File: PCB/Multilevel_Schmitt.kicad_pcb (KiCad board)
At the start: 2 copper layers, 55 x 70 mm, 26 parts, among them J1 Analog IO, J2 I2C input, J3 Conn_01x08_Female, J4 Conn_01x08_Female, J5 Conn_01x02_Female, U1 ATtiny84-20PU, U2 74HC14, U3 MCP1700-2502E_TO92, U4 74HC4051, U5 74HC4051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

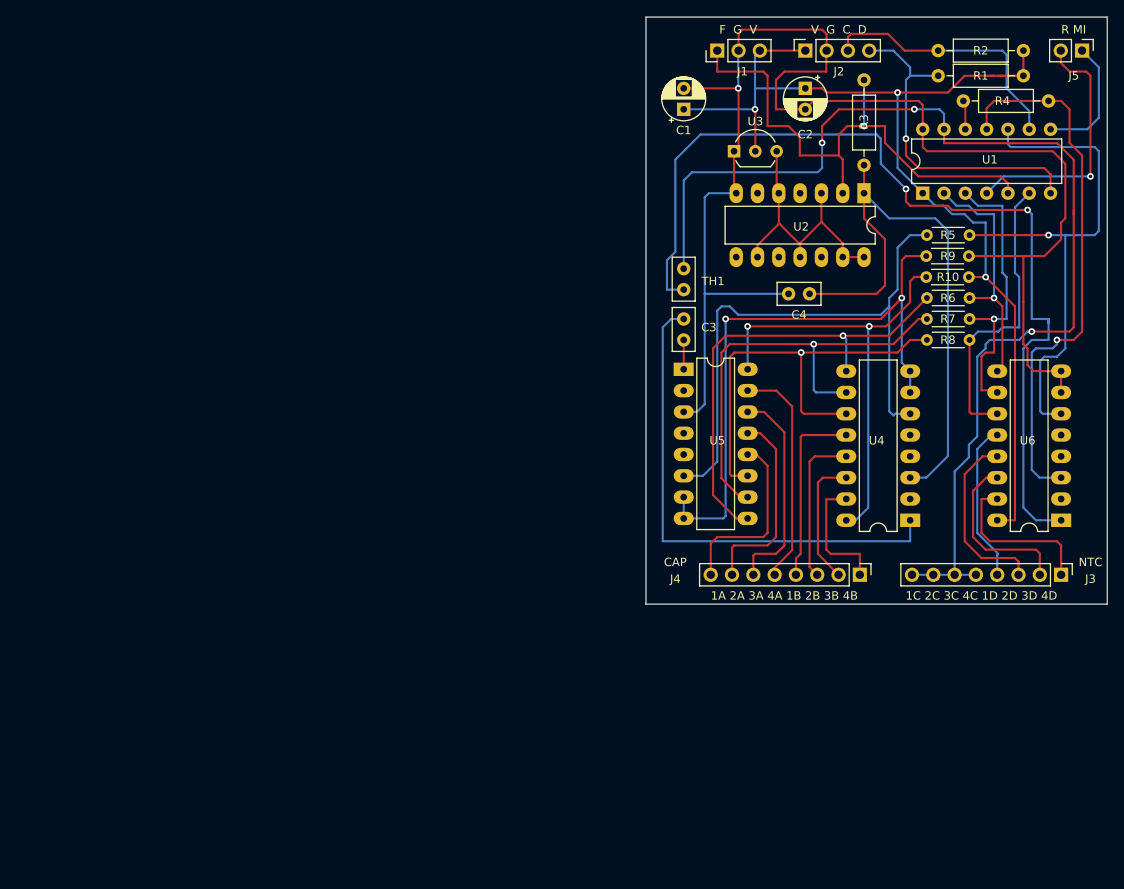
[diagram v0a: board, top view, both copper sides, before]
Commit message: Updates PCB design files, removed casing files and updates readme files
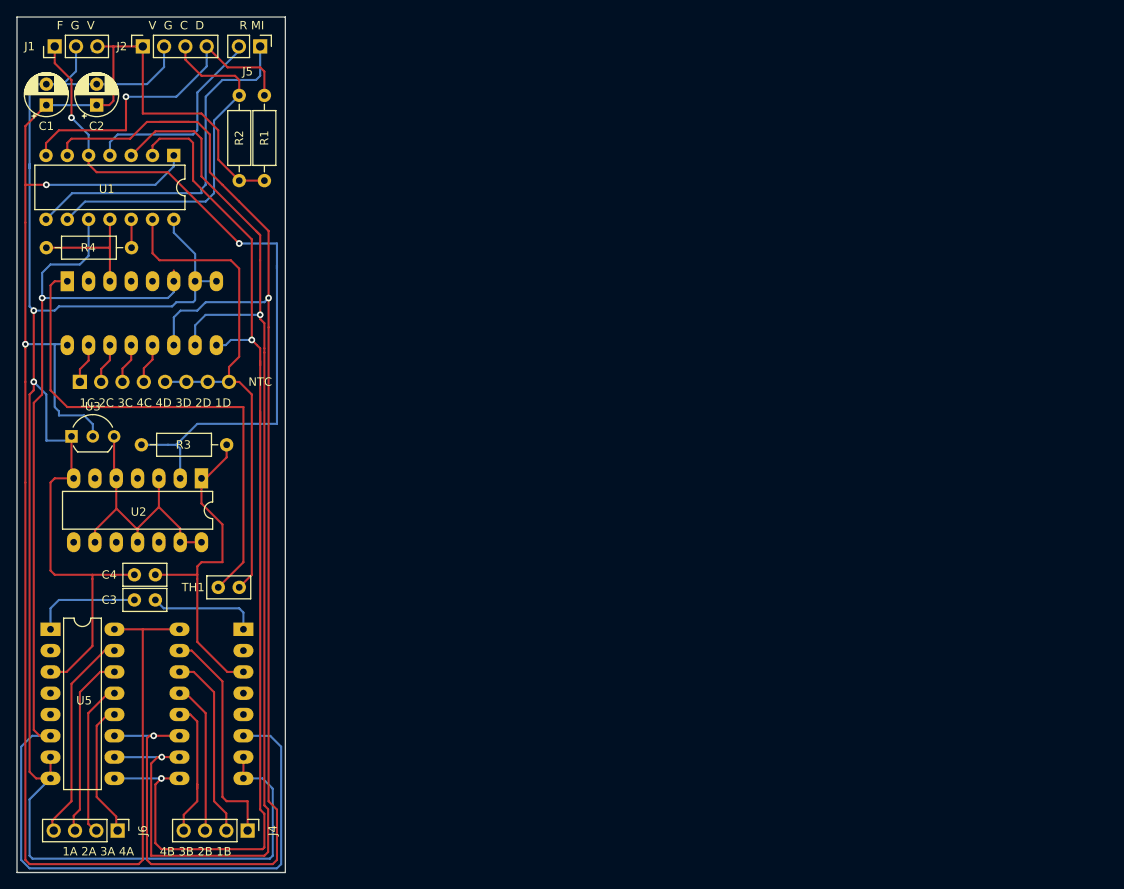
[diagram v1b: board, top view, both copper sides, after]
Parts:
- removed R10, R5, R6, R7, R8, R9: R, Resistor_THT:R_Axial_DIN0204_L3.6mm_D1.6mm_P5.08mm_Horizontal
- added J6: Conn_01x04_Female, Connector_PinHeader_2.54mm:PinHeader_1x04_P2.54mm_Vertical, F.Cu at (112.0, 147.0)
- J3, U4, U6: moved to B.Cu
- J4: value Conn_01x08_Female -> Conn_01x04_Female; footprint Connector_PinHeader_2.54mm:PinHeader_1x08_P2.54mm_Vertical -> Connector_PinHeader_2.54mm:PinHeader_1x04_P2.54mm_Vertical
- moved U6 121.9 mm to (106.0, 81.5), turned to 270 degrees
- moved R4 120.8 mm to (103.5, 77.5), turned to 0 degrees
- moved J3 119.2 mm to (107.5, 93.5)
- moved J5 98.0 mm to (129.0, 53.5)
- moved R2 94.8 mm to (126.5, 69.5), turned to 90 degrees
- moved R1 91.4 mm to (129.5, 69.5), turned to 90 degrees
- moved U1 89.4 mm to (118.7, 66.5), turned to 270 degrees
- moved U2 86.0 mm to (122.0, 105.0)
- moved U3 86.0 mm to (106.5, 100.0)
- moved C4 84.9 mm to (116.5, 116.5)
- moved C2 84.5 mm to (109.5, 60.5), turned to 90 degrees
- moved R3 83.0 mm to (125.0, 101.0), turned to 180 degrees
- moved U5 81.6 mm to (104.0, 123.0)
- moved U4 80.6 mm to (127.0, 123.0)
- moved J4 79.1 mm to (127.5, 147.0)
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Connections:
- U4 pad 10: Net-(R7-Pad1) -> S1
- U4 pad 11: Net-(R8-Pad1) -> S0
- U4 pad 16: 3V3 -> +3V3
- U4 pad 6: Net-(R5-Pad1) -> E
- U4 pad 7: GND2 -> M0
- U4 pad 8: GND2 -> M0
- U4 pad 9: Net-(R6-Pad1) -> S2
- U5 pad 10: Net-(R7-Pad1) -> S1
- U5 pad 11: Net-(R8-Pad1) -> S0
- U5 pad 12: Net-(J4-Pad8) -> Net-(J6-Pad1)
- U5 pad 13: Net-(J4-Pad7) -> Net-(J6-Pad2)
- U5 pad 14: Net-(J4-Pad6) -> Net-(J6-Pad3)
- U5 pad 15: Net-(J4-Pad5) -> Net-(J6-Pad4)
- U5 pad 16: 3V3 -> +3V3
- U5 pad 6: Net-(R5-Pad1) -> E
- U5 pad 7: GND2 -> M0
- U5 pad 8: GND2 -> M0
- U5 pad 9: Net-(R6-Pad1) -> S2
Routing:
- net S0: track 35.7 -> 168.1 mm, vias 0 -> 2
- net S1: track 35.8 -> 144.1 mm, vias 1 -> 2
- net +3V3: track 127.6 -> 229.1 mm, vias 3 -> 2
- net S2: track 29.4 -> 129.7 mm, vias 1 -> 2
- net E: track 63.8 -> 155.8 mm
- net M0: track 176.7 -> 256.8 mm, vias 1 -> 2
- net NTC_H: track 136.5 -> 63.7 mm, vias 3 -> 0
- net GND2: track 72.5 -> 0.00 mm, vias 2 -> 0
- net Net-(R5-Pad1): track 71.9 -> 0.00 mm
- net Net-(R7-Pad1): track 55.4 -> 0.00 mm, vias 1 -> 0
- net Net-(R6-Pad1): track 55.3 -> 0.00 mm, vias 1 -> 0
- net 3V3: track 55.2 -> 0.00 mm, vias 2 -> 0
- net Net-(R8-Pad1): track 53.0 -> 0.00 mm, vias 1 -> 0
- net TR: track 113.3 -> 61.3 mm, vias 2 -> 0
- net A5: track 66.2 -> 15.0 mm, vias 1 -> 0
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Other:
- board size 55 x 70 mm -> 32 x 102 mm
- board text added: "1A 2A 3A 4A 4B 3B 2B 1B"
- board text added: "1C 2C 3C 4C 4D 3D 2D 1D"
- board text removed: "1A 2A 3A 4A 1B 2B 3B 4B"
- board text removed: "1C 2C 3C 4C 1D 2D 3D 4D"
- board text removed: "CAP"

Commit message: latest changes to PCB design
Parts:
- C3, C4: footprint Capacitor_THT:C_Disc_D5.0mm_W2.5mm_P2.50mm -> Capacitor_THT:C_Disc_D5.0mm_W2.5mm_P5.00mm
- J1: value Analog IO -> Conn_01x04; footprint Connector_PinHeader_2.54mm:PinHeader_1x03_P2.54mm_Vertical -> Connector_PinHeader_2.54mm:PinHeader_1x04_P2.54mm_Vertical
- U2: footprint Package_DIP:DIP-14_W7.62mm_LongPads -> Package_DIP:DIP-14_W7.62mm
- U4, U5, U6: footprint Package_DIP:DIP-16_W7.62mm_LongPads -> Package_DIP:DIP-16_W7.62mm
- moved J1 6.50 mm to (111.0, 53.5), turned to 270 degrees
- moved C3 1.00 mm to (117.5, 119.5)
- moved C4 1.00 mm to (117.5, 116.5)
- moved J3 1.00 mm to (107.5, 94.5)
- moved U3 0.50 mm to (106.5, 100.5)
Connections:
- net A5 renamed A2
- C1 pad 1: +3V3 -> VCC
- C1 pad 2: M0 -> E
- C2 pad 1: +3V3 -> VCC
- C2 pad 2: M0 -> E
- C4 pad 2: M0 -> E
- J1 pad 1: F_OUT -> +3V3
- J1 pad 2: M0 -> VCC
- J1 pad 3: +3V3 -> A3
- J2 pad 2: M0 -> E
- R1 pad 1: +3V3 -> VCC
- R2 pad 1: +3V3 -> VCC
- U1 pad 1: +3V3 -> VCC
- U1 pad 10: E -> A3
- U1 pad 14: M0 -> E
- U2 pad 11: +2V5 -> A3
- U2 pad 13: +2V5 -> A3
- U2 pad 14: +2V5 -> A3
- U2 pad 3: +2V5 -> A3
- U2 pad 5: +2V5 -> A3
- U2 pad 7: M0 -> E
- U2 pad 9: +2V5 -> A3
- U3 pad 1: M0 -> E
- U3 pad 3: +2V5 -> A3
- U4 pad 4: Net-(U4-Pad4) -> VCC
- U4 pad 7: M0 -> E
- U4 pad 8: M0 -> E
- U5 pad 3: M0 -> E
- U5 pad 4: Net-(U5-Pad4) -> E
- U5 pad 7: M0 -> E
- U5 pad 8: M0 -> E
- U6 pad 12: Net-(J3-Pad4) -> Net-(J3-Pad1)
- U6 pad 13: Net-(J3-Pad3) -> Net-(J3-Pad2)
- U6 pad 14: Net-(J3-Pad2) -> Net-(J3-Pad3)
- U6 pad 15: Net-(J3-Pad1) -> Net-(J3-Pad4)
- U6 pad 7: M0 -> E
- U6 pad 8: M0 -> E
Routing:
- net M0: track 256.8 -> 0.00 mm, vias 2 -> 0
- net A3: track 0.00 -> 122.4 mm, vias 0 -> 3
- net VCC: track 0.00 -> 118.0 mm, vias 0 -> 2
- net E: track 155.8 -> 258.2 mm, vias 1 -> 3
- net +3V3: track 229.1 -> 182.2 mm, vias 2 -> 1
- net +2V5: track 33.8 -> 0.00 mm
- net Net-(J3-Pad4): track 4.87 -> 35.3 mm
- net Net-(J3-Pad1): track 4.87 -> 13.1 mm
- net Net-(J3-Pad3): track 4.87 -> 8.19 mm, vias 0 -> 1
- net RESET: track 24.6 -> 22.0 mm
- net Net-(J3-Pad2): track 4.87 -> 7.45 mm
- net SDA: track 40.1 -> 37.8 mm
- net F_OUT: track 85.5 -> 83.6 mm, vias 2 -> 1
- net CR_L: track 12.9 -> 11.4 mm
- net NTC_H: track 63.7 -> 65.2 mm
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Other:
- board text added: "3 G C D"
- board text added: "4C 4C 2C 1C 1D 2D 3D 4D"
- board text added: "F 2.5 V 3"
- board text removed: "1C 2C 3C 4C 4D 3D 2D 1D"
- board text removed: "F G V"
- board text removed: "V G C D"

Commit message: start with flex version
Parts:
- removed J1: Conn_01x04, Connector_PinHeader_2.54mm:PinHeader_1x04_P2.54mm_Vertical
- removed J6: Conn_01x04_Female, Connector_PinHeader_2.54mm:PinHeader_1x04_P2.54mm_Vertical
- added R5: R, Resistor_THT:R_Axial_DIN0207_L6.3mm_D2.5mm_P10.16mm_Horizontal, F.Cu at (121.5, 113.5)
- C1: footprint Capacitor_THT:CP_Radial_D5.0mm_P2.50mm -> Capacitor_THT:C_Disc_D5.0mm_W2.5mm_P2.50mm
- C3, C4: footprint Capacitor_THT:C_Disc_D5.0mm_W2.5mm_P5.00mm -> Resistor_THT:R_Axial_DIN0207_L6.3mm_D2.5mm_P10.16mm_Horizontal
- J3: footprint Connector_PinHeader_2.54mm:PinHeader_1x08_P2.54mm_Vertical -> Connector_PinHeader_1.00mm:PinHeader_1x08_P1.00mm_Vertical; moved to F.Cu
- J4: value Conn_01x04_Female -> Conn_01x08_Female; footprint Connector_PinHeader_2.54mm:PinHeader_1x04_P2.54mm_Vertical -> Connector_PinHeader_1.00mm:PinHeader_1x08_P1.00mm_Vertical
- U4, U6: moved to F.Cu
- moved J3 54.2 mm to (112.5, 148.5), turned to 90 degrees
- moved U6 35.1 mm to (129.0, 108.0), turned to 180 degrees
- moved R4 21.9 mm to (123.5, 86.5), turned to 90 degrees
- moved U2 21.6 mm to (103.5, 93.8), turned to 0 degrees
- moved U4 19.1 mm to (129.0, 142.0)
- moved R1 17.0 mm to (130.0, 86.5)
- moved R2 17.0 mm to (127.0, 86.5)
- moved R3 17.0 mm to (113.0, 89.0)
- moved U3 16.4 mm to (103.0, 84.5)
- moved C2 16.0 mm to (105.5, 76.0)
- moved J4 14.5 mm to (113.0, 146.5), turned to 90 degrees
- moved C1 8.06 mm to (104.5, 68.5), turned to 0 degrees
- moved U1 6.51 mm to (112.5, 68.5), turned to 0 degrees
- moved C3 4.00 mm to (121.5, 119.5)
- moved C4 4.00 mm to (121.5, 116.5)
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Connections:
- C1 pad 1: VCC -> +2V5
- C1 pad 2: E -> M0
- C2 pad 1: VCC -> +2V5
- C2 pad 2: E -> M0
- C4 pad 2: E -> M0
- J2 pad 2: E -> M0
- J3 pad 1: Net-(J3-Pad1) -> C0_A1
- J3 pad 2: Net-(J3-Pad2) -> C0_A2
- J3 pad 3: Net-(J3-Pad3) -> NTC_A3
- J3 pad 4: Net-(J3-Pad4) -> NTC_A0
- J3 pad 7: NTC_H -> C1_A3
- J3 pad 8: NTC_H -> C1_A0
- J4 pad 1: Net-(J4-Pad1) -> C0_A0
- J4 pad 2: Net-(J4-Pad2) -> C0_A3
- J4 pad 3: Net-(J4-Pad3) -> NTC_A2
- J4 pad 4: Net-(J4-Pad4) -> NTC_A1
- R1 pad 1: VCC -> +2V5
- R2 pad 1: VCC -> +2V5
- R3 pad 1: M1 -> Net-(R3-Pad1)
- U1 pad 1: VCC -> +2V5
- U1 pad 14: E -> M0
- U2 pad 1: M1 -> Net-(R3-Pad1)
- U2 pad 11: A3 -> +2V5
- U2 pad 13: A3 -> +2V5
- U2 pad 14: A3 -> +2V5
- U2 pad 3: A3 -> M0
- U2 pad 5: A3 -> M0
- U2 pad 7: E -> M0
- U2 pad 9: A3 -> +2V5
- U3 pad 1: E -> M0
- U3 pad 3: A3 -> +2V5
- U4 pad 12: Net-(J4-Pad4) -> C1_A3
- U4 pad 13: Net-(J4-Pad3) -> C1_A0
- U4 pad 14: Net-(J4-Pad2) -> C1_A1
- U4 pad 15: Net-(J4-Pad1) -> C1_A2
- U4 pad 16: +3V3 -> +2V5
- U4 pad 4: VCC -> +2V5
- U4 pad 6: E -> M0
- U4 pad 7: E -> M0
- U4 pad 8: E -> M0
- U5 pad 12: Net-(J6-Pad1) -> C0_A3
- U5 pad 13: Net-(J6-Pad2) -> C0_A0
- U5 pad 14: Net-(J6-Pad3) -> C0_A1
- U5 pad 15: Net-(J6-Pad4) -> C0_A2
- U5 pad 16: +3V3 -> +2V5
- U5 pad 3: E -> M0
- U5 pad 4: E -> M0
- U5 pad 6: E -> M0
- U5 pad 7: E -> M0
- U5 pad 8: E -> M0
- U6 pad 12: Net-(J3-Pad1) -> NTC_A3
- U6 pad 13: Net-(J3-Pad2) -> NTC_A0
- U6 pad 14: Net-(J3-Pad3) -> NTC_A1
- U6 pad 15: Net-(J3-Pad4) -> NTC_A2
- U6 pad 16: +3V3 -> +2V5
- U6 pad 6: E -> M0
- U6 pad 7: E -> M0
- U6 pad 8: E -> M0
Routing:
- net E: track 258.2 -> 0.00 mm, vias 3 -> 0
- net +3V3: track 182.2 -> 0.00 mm, vias 1 -> 0
- net A3: track 122.4 -> 0.00 mm, vias 3 -> 0
- net VCC: track 118.0 -> 0.00 mm, vias 2 -> 1
- net S0: track 168.1 -> 50.2 mm, vias 2 -> 0
- net +2V5: track 0.00 -> 117.1 mm
- net M0: track 0.00 -> 113.8 mm
- net S1: track 144.1 -> 52.7 mm, vias 2 -> 0
- net F_OUT: track 83.6 -> 9.39 mm, vias 1 -> 0
- net S2: track 130.9 -> 57.4 mm, vias 2 -> 0
- net TR: track 62.4 -> 5.71 mm
- net MISO: track 43.1 -> 0.50 mm
- net SCL: track 42.7 -> 1.69 mm
- net Net-(R3-Pad1): track 0.00 -> 37.5 mm
- net C0_A2: track 0.00 -> 36.1 mm
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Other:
- board text removed: "1A 2A 3A 4A 4B 3B 2B 1B"
- board text removed: "4C 4C 2C 1C 1D 2D 3D 4D"
- board text removed: "NTC"
